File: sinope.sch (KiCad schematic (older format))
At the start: 46 parts, among them J1 PIOA, J2 SERIAL0, J3 PIOB, J4 SERIAL1, J5 Battery, J6 5VDC, Q1 3N3906, SW1 RESET, U1 Z80CPU, U10 MEMORY_GAL, U11 74LS157, U12 TC551001, U2 Z80CTC, U3 Z80PIO, U4 Z80SIO, U5 MAX232, U6 MAX232, U7 IO_GAL, U8 MAX695, U9 27C010, X1 3.6864Mhz

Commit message: PCB mostly routed
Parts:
- removed J4: SERIAL1, Connector_Dsub:DSUB-9_Male_EdgeMount_P2.77mm, symbol Connector:DB9_Male
- added J4: SERIAL1, Connector_PinHeader_2.54mm:PinHeader_1x03_P2.54mm_Vertical, symbol Connector:Conn_01x03_Male
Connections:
- wire segments 410 -> 405
- no-connect marks 37 -> 31
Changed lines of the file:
@@
 $Descr A3 16535 11693
 encoding utf-8
-Sheet 1 2
+Sheet 1 1
 Title "sinope Z80 Single Board Computer"
 Date "2020-04-16"
@@
 	1    0    0    -1
 $EndComp
-NoConn ~ 15200 4000
-NoConn ~ 15200 3900
-NoConn ~ 15200 3700
-NoConn ~ 15200 3500
-NoConn ~ 15200 3400
-NoConn ~ 15200 3300
 NoConn ~ 15200 2200
 NoConn ~ 15200 1600
@@
 	14000 2200 14100 2200
 Wire Wire Line
-	14900 1700 14900 3900
-Wire Wire Line
-	14900 1700 15200 1700
-Wire Wire Line
 	14000 2100 15200 2100
 Wire Wire Line
@@
 Wire Wire Line
 	14000 1900 15200 1900
-Wire Wire Line
-	15000 2300 15000 4100
-Wire Wire Line
-	15000 2300 15200 2300
-Wire Wire Line
-	14750 3200 15200 3200
-$Comp
-L power:GND #PWR019
-U 1 1 5F911907
-P 14750 3200
-F 0 "#PWR019" H 14750 2950 50  0001 C CNN
-F 1 "GND" H 14750 3050 50  0000 C CNN
-F 2 "" H 14750 3200 50  0001 C CNN
-F 3 "" H 14750 3200 50  0001 C CNN
-	1    14750 3200
-	1    0    0    -1
-$EndComp
 Text Label 14350 4200 2    50   ~ 0
 RxDB
 Text Label 14350 4000 2    50   ~ 0
 TxDB
-Wire Wire Line
-	14800 3600 15200 3600
-Wire Wire Line
-	14800 4000 14800 3600
-Wire Wire Line
-	14000 4000 14800 4000
-Wire Wire Line
-	15100 3800 15200 3800
-Wire Wire Line
-	15100 4200 15100 3800
-Wire Wire Line
-	14000 4200 15100 4200
 Text Label 14350 3900 2    50   ~ 0
 DTRA
@@
 Wire Wire Line
 	14000 4100 15000 4100
-$Comp
-L Connector:DB9_Male J4
-U 1 1 5F8AE309
-P 15500 3600
-F 0 "J4" H 15680 3646 50  0000 L CNN
-F 1 "SERIAL1" H 15680 3555 50  0000 L CNN
-F 2 "Connector_Dsub:DSUB-9_Male_EdgeMount_P2.77mm" H 15500 3600 50  0001 C CNN
-F 3 " ~" H 15500 3600 50  0001 C CNN
-	1    15500 3600
-	1    0    0    -1
-$EndComp
 $Comp
 L Connector:DB9_Male J2
@@
 Wire Wire Line
 	12900 3300 12900 3200
-Wire Wire Line
-	13100 3300 12900 3300
 Wire Wire Line
 	12900 3400 13100 3400
@@
 Wire Wire Line
 	1250 3000 1850 3000
-Text GLabel 12600 9150 0    50   Input ~ 0
+Text GLabel 13950 9150 2    50   Input ~ 0
 RAMVCC
 Text GLabel 4850 7700 2    50   Output ~ 0
@@
 	11800 2300 12500 2300
 Wire Wire Line
-	12500 2300 12500 4200
-Wire Wire Line
-	12500 4200 13100 4200
-Wire Wire Line
 	11800 2500 12450 2500
-Wire Wire Line
-	12450 2500 12450 4000
-Wire Wire Line
-	12450 4000 13100 4000
 Text GLabel 4700 2100 0    50   Input ~ 0
 ~CTCCS
@@
 Wire Wire Line
 	13050 9150 13050 9350
-Wire Wire Line
-	12600 9150 13050 9150
 Wire Wire Line
 	13050 6550 13050 6500
@@
 	1    0    0    -1
 $EndComp
+Wire Wire Line
+	13850 9150 13950 9150
+Connection ~ 13850 9150
+Wire Wire Line
+	15000 2300 15200 2300
+Wire Wire Line
+	15000 2300 15000 4100
+Wire Wire Line
+	14900 1700 14900 3900
+Wire Wire Line
+	14900 1700 15200 1700
+Wire Wire Line
+	13100 3300 12900 3300
+$Comp
+L Connector:Conn_01x03_Male J4
+U 1 1 5EAC89FF
+P 15400 5000
+F 0 "J4" H 15508 5281 50  0000 C CNN
+F 1 "SERIAL1" H 15508 5190 50  0000 C CNN
+F 2 "Connector_PinHeader_2.54mm:PinHeader_1x03_P2.54mm_Vertical" H 15400 5000 50  0001 C CNN
+F 3 "~" H 15400 5000 50  0001 C CNN
+	1    15400 5000
+	-1   0    0    -1
+$EndComp
+Wire Wire Line
+	12500 4900 15200 4900
+Wire Wire Line
+	12500 2300 12500 4900
+Wire Wire Line
+	12450 5000 15200 5000
+Wire Wire Line
+	12450 2500 12450 5000
+$Comp
+L power:GND #PWR0101
+U 1 1 5ED291FA
+P 15100 5150
+F 0 "#PWR0101" H 15100 4900 50  0001 C CNN
+F 1 "GND" H 15100 5000 50  0000 C CNN
+F 2 "" H 15100 5150 50  0001 C CNN
+F 3 "" H 15100 5150 50  0001 C CNN
+	1    15100 5150
+	1    0    0    -1
+$EndComp
+Wire Wire Line
+	15100 5150 15100 5100
+Wire Wire Line
+	15100 5100 15200 5100
 Wire Bus Line
 	5800 8250 5800 10250

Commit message: PCB routed
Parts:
- removed J2: SERIAL0, Connector_Dsub:DSUB-9_Male_EdgeMount_P2.77mm, symbol Connector:DB9_Male
- added J2: SERIAL0, Connector_PinHeader_2.00mm:PinHeader_2x05_P2.00mm_Vertical, symbol Connector_Generic:Conn_02x05_Top_Bottom
- SW1: footprint Button_Switch_THT:Push_E-Switch_KS01Q01 -> Connector_PinHeader_2.54mm:PinHeader_1x02_P2.54mm_Vertical
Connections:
- net labels removed: RxDB, TxDB
- wire segments 405 -> 412
- no-connect marks 31 -> 36
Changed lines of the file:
@@
 	1    0    0    -1
 $EndComp
-NoConn ~ 15200 2200
-NoConn ~ 15200 1600
-Wire Wire Line
-	14750 1500 15200 1500
 $Comp
 L power:GND #PWR09
 U 1 1 5FA2F101
-P 14750 1500
-F 0 "#PWR09" H 14750 1250 50  0001 C CNN
-F 1 "GND" H 14750 1350 50  0000 C CNN
-F 2 "" H 14750 1500 50  0001 C CNN
-F 3 "" H 14750 1500 50  0001 C CNN
-	1    14750 1500
-	1    0    0    -1
-$EndComp
-Wire Wire Line
-	14100 1800 15200 1800
-Wire Wire Line
-	14100 2200 14100 1800
-Wire Wire Line
-	14000 2200 14100 2200
-Wire Wire Line
-	14000 2100 15200 2100
-Wire Wire Line
-	14000 2000 15200 2000
-Wire Wire Line
-	14000 1900 15200 1900
-Text Label 14350 4200 2    50   ~ 0
-RxDB
-Text Label 14350 4000 2    50   ~ 0
-TxDB
-Text Label 14350 3900 2    50   ~ 0
+P 14550 3100
+F 0 "#PWR09" H 14550 2850 50  0001 C CNN
+F 1 "GND" H 14550 2950 50  0000 C CNN
+F 2 "" H 14550 3100 50  0001 C CNN
+F 3 "" H 14550 3100 50  0001 C CNN
+	1    14550 3100
+	1    0    0    -1
+$EndComp
+Text Label 14250 3900 2    50   ~ 0
 DTRA
-Text Label 14350 4100 2    50   ~ 0
+Text Label 14250 4100 2    50   ~ 0
 DCDA
-Wire Wire Line
-	14000 3900 14900 3900
-Wire Wire Line
-	14000 4100 15000 4100
-$Comp
-L Connector:DB9_Male J2
-U 1 1 5F8ABC1E
-P 15500 1900
-F 0 "J2" H 15680 1946 50  0000 L CNN
-F 1 "SERIAL0" H 15680 1855 50  0000 L CNN
-F 2 "Connector_Dsub:DSUB-9_Male_EdgeMount_P2.77mm" H 15500 1900 50  0001 C CNN
-F 3 " ~" H 15500 1900 50  0001 C CNN
-	1    15500 1900
-	1    0    0    -1
-$EndComp
 Connection ~ 13550 2950
 Wire Wire Line
@@
 P 14200 3300
 F 0 "#PWR020" H 14200 3050 50  0001 C CNN
-F 1 "GND" V 14200 3100 50  0000 C CNN
+F 1 "GND" H 14300 3200 50  0000 C CNN
 F 2 "" H 14200 3300 50  0001 C CNN
 F 3 "" H 14200 3300 50  0001 C CNN
 	1    14200 3300
-	0    -1   -1   0
+	1    0    0    -1
 $EndComp
 $Comp
@@
 Text Label 3400 3800 0    50   ~ 0
 A15
-Text Label 14150 1800 0    50   ~ 0
+Text Label 14050 2200 0    50   ~ 0
 CTSA
-Text Label 14150 1900 0    50   ~ 0
+Text Label 14050 1900 0    50   ~ 0
 TxDA
-Text Label 14150 2000 0    50   ~ 0
+Text Label 14050 2000 0    50   ~ 0
 RTSA
-Text Label 14150 2100 0    50   ~ 0
+Text Label 14050 2100 0    50   ~ 0
 RxDA
 Wire Wire Line
@@
 F 0 "SW1" H 4500 10035 50  0000 C CNN
 F 1 "RESET" H 4500 9944 50  0000 C CNN
-F 2 "Button_Switch_THT:Push_E-Switch_KS01Q01" H 4500 9950 50  0001 C CNN
+F 2 "Connector_PinHeader_2.54mm:PinHeader_1x02_P2.54mm_Vertical" H 4500 9950 50  0001 C CNN
 F 3 "~" H 4500 9950 50  0001 C CNN
 	1    4500 9750
@@
 Connection ~ 13850 9150
 Wire Wire Line
-	15000 2300 15200 2300
-Wire Wire Line
-	15000 2300 15000 4100
-Wire Wire Line
-	14900 1700 14900 3900
-Wire Wire Line
-	14900 1700 15200 1700
-Wire Wire Line
 	13100 3300 12900 3300
 $Comp
@@
 Wire Wire Line
 	15100 5100 15200 5100
+$Comp
+L Connector_Generic:Conn_02x05_Top_Bottom J2
+U 1 1 5EA81F1E
+P 14800 2850
+F 0 "J2" H 14850 3267 50  0000 C CNN
+F 1 "SERIAL0" H 14850 3176 50  0000 C CNN
+F 2 "Connector_PinHeader_2.00mm:PinHeader_2x05_P2.00mm_Vertical" H 14800 2850 50  0001 C CNN
+F 3 "~" H 14800 2850 50  0001 C CNN
+	1    14800 2850
+	1    0    0    -1
+$EndComp
+Wire Wire Line
+	14000 2100 14300 2100
+Wire Wire Line
+	14300 2100 14300 2750
+Wire Wire Line
+	14300 2750 14600 2750
+Wire Wire Line
+	14000 1900 14350 1900
+Wire Wire Line
+	14350 1900 14350 2850
+Wire Wire Line
+	14350 2850 14600 2850
+Wire Wire Line
+	14000 3900 14350 3900
+Wire Wire Line
+	14350 3900 14350 2950
+Wire Wire Line
+	14350 2950 14600 2950
+Wire Wire Line
+	14600 3050 14550 3050
+Wire Wire Line
+	14550 3050 14550 3100
+NoConn ~ 15100 2650
+Wire Wire Line
+	15200 2000 15200 2750
+Wire Wire Line
+	15200 2750 15100 2750
+Wire Wire Line
+	14000 2000 15200 2000
+Wire Wire Line
+	15150 2200 15150 2850
+Wire Wire Line
+	15150 2850 15100 2850
+Wire Wire Line
+	14000 2200 15150 2200
+NoConn ~ 15100 2950
+NoConn ~ 15100 3050
+Wire Wire Line
+	14000 4100 14400 4100
+Wire Wire Line
+	14400 4100 14400 2650
+Wire Wire Line
+	14400 2650 14600 2650
+NoConn ~ 14000 4000
+NoConn ~ 14000 4200
+NoConn ~ 13100 4200
+NoConn ~ 13100 4000
 Wire Bus Line
 	5800 8250 5800 10250

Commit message: Move connectors to one side.
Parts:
- added J7: Z80_BUS, Connector_PinSocket_2.54mm:PinSocket_1x40_P2.54mm_Vertical, symbol sinope:Z80_BUS
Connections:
- wire segments 412 -> 450
- no-connect marks 36 -> 41
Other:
- moved on the sheet: C16, C17, C18, C19, C20, C21, C22, D1, J5, J6, Q1, R2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

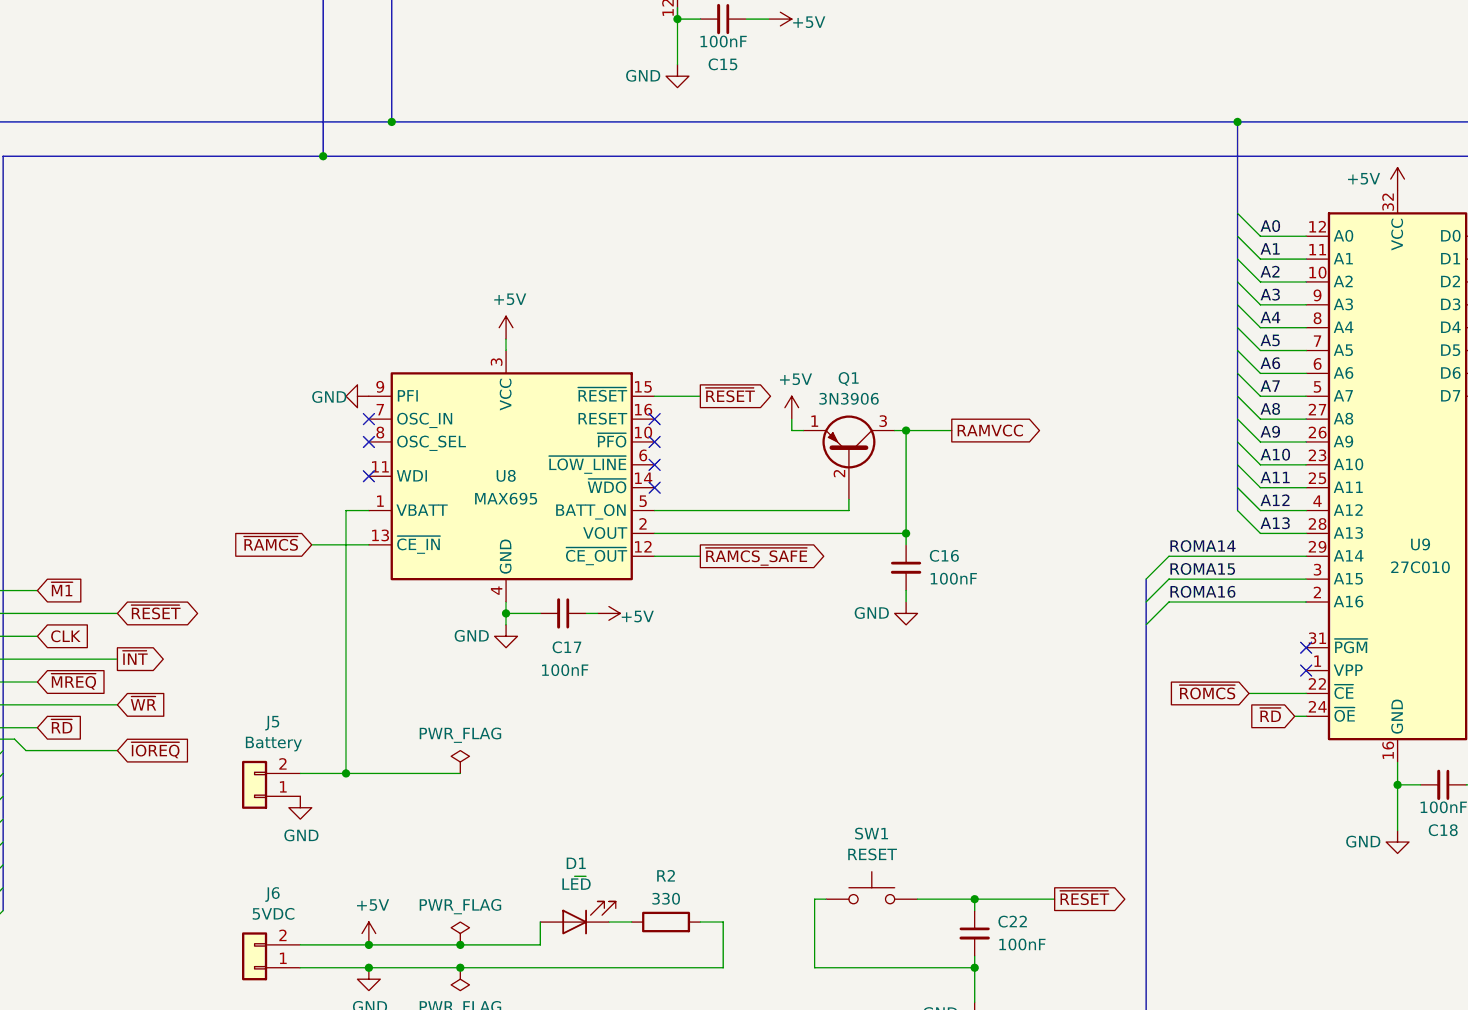
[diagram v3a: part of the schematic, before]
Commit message: ROM variant jumpers and cleanup, sent to JLCPCB for production
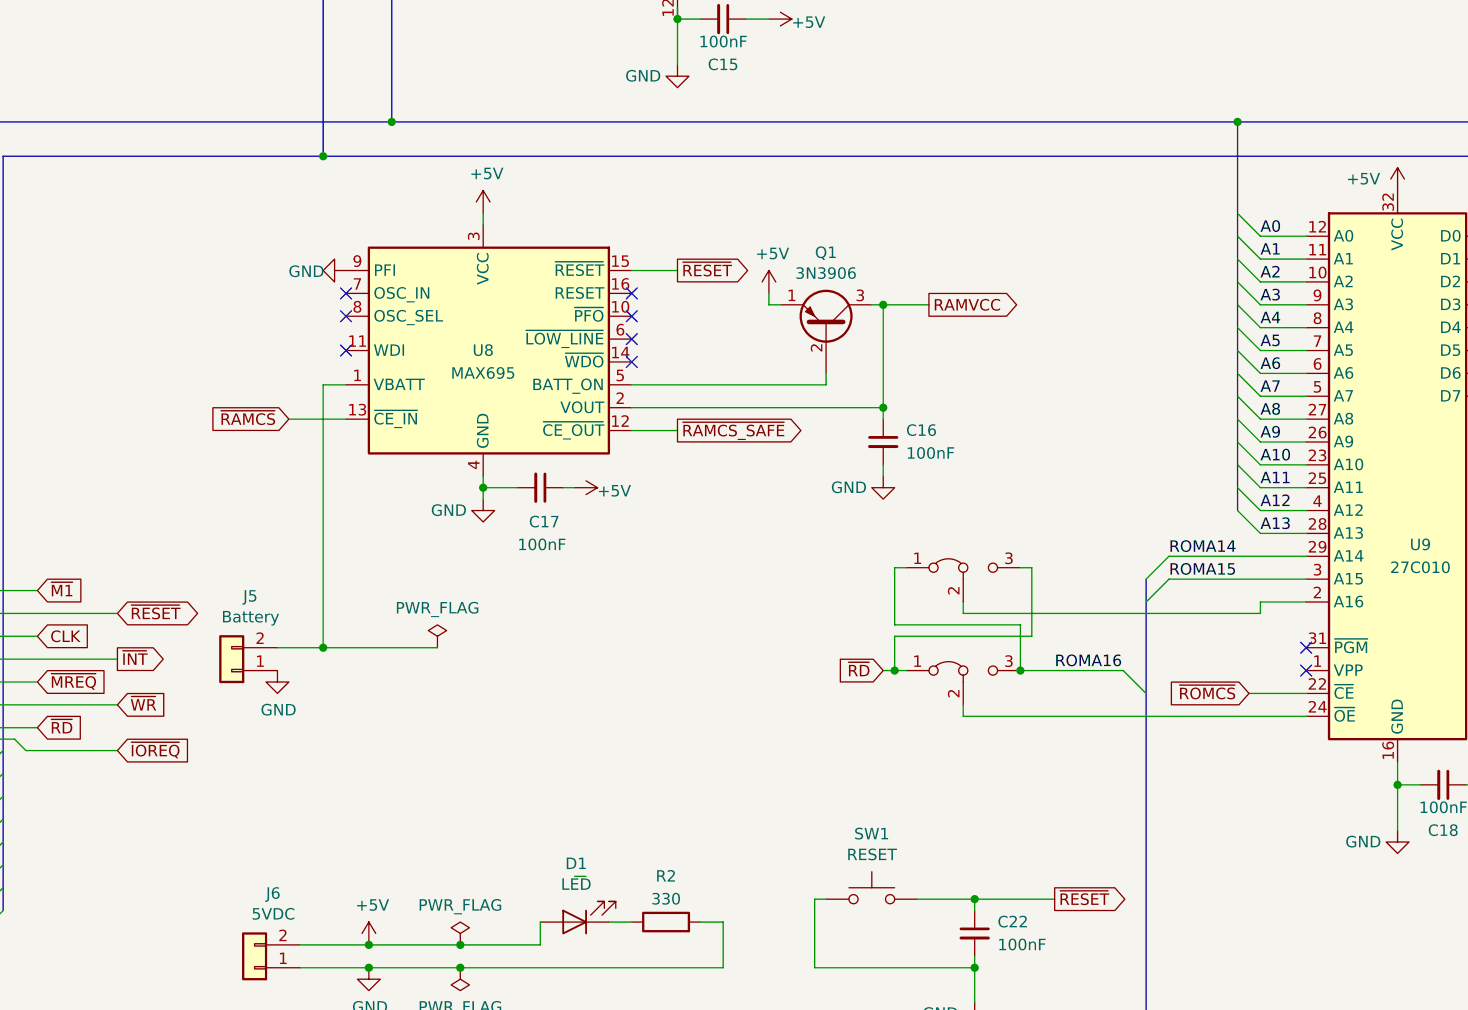
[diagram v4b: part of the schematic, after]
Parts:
- added JP1, JP2: Jumper_3_Bridged12, Connector_PinHeader_2.54mm:PinHeader_1x03_P2.54mm_Vertical, symbol Jumper:Jumper_3_Bridged12
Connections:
- wire segments 450 -> 465
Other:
- moved on the sheet: C16, C17, J5, Q1, U8

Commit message: Begin work on v2
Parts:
- removed C12, C13, C8: 100nF, Capacitor_SMD:C_0805_2012Metric, symbol Device:C_Small
- removed J4: SERIAL1, Connector_PinHeader_2.54mm:PinHeader_1x03_P2.54mm_Vertical, symbol Connector:Conn_01x03_Male
- removed J5: Battery, Connector_PinHeader_2.54mm:PinHeader_2x01_P2.54mm_Vertical, symbol Connector_Generic:Conn_01x02
- removed J6: 5VDC, Connector_PinHeader_2.54mm:PinHeader_1x02_P2.54mm_Vertical, symbol Connector_Generic:Conn_01x02
- removed JP1, JP2: Jumper_3_Bridged12, Connector_PinHeader_2.54mm:PinHeader_1x03_P2.54mm_Vertical, symbol Jumper:Jumper_3_Bridged12
- removed U6: MAX232, Package_DIP:DIP-16_W7.62mm, symbol sinope:MAX232
- added BT1: Battery, Battery:Battery_Panasonic_CR2032-VS1N_Vertical_CircularHoles, symbol Device:Battery_Cell
- added D2, D3: LED, LED_SMD:LED_0805_2012Metric, symbol Device:LED
- added J4: USB_B_Micro, Connector_USB:USB_Micro-B_Molex-105017-0001, symbol Connector:USB_B_Micro
- added JP1, JP2: SolderJumper_3_Bridged12, Connector_PinHeader_2.54mm:PinHeader_1x03_P2.54mm_Vertical, symbol Jumper:SolderJumper_3_Bridged12
- added R3, R4: 330, Resistor_SMD:R_0805_2012Metric, symbol Device:R
- added R5, R6, R7: 3k3, Resistor_SMD:R_0805_2012Metric, symbol Device:R
- added U6: FT232RL, Package_SO:SSOP-28_5.3x10.2mm_P0.65mm, symbol sinope:FT232RL
- J2: value SERIAL0 -> SERIAL1; footprint Connector_PinHeader_2.00mm:PinHeader_2x05_P2.00mm_Vertical -> Connector_PinHeader_2.54mm:PinHeader_2x05_P2.54mm_Vertical
- J7: footprint Connector_PinSocket_2.54mm:PinSocket_1x40_P2.54mm_Vertical -> Connector_PinSocket_2.54mm:PinSocket_1x39_P2.54mm_Vertical
- Q1: value 3N3906 -> MMBT3904; footprint Package_TO_SOT_THT:TO-92 -> Package_TO_SOT_SMD:SOT-23
- SW1: footprint Connector_PinHeader_2.54mm:PinHeader_1x02_P2.54mm_Vertical -> Button_Switch_SMD:SW_SPST_PTS645
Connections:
- net labels added: RxDB, SPARE1, SPARE2, SPARE3, TxDB, USB_D+, USB_D-, ~BUSACK, ~BUSRQ, ~HALT, ~NMI, ~RFSH, ~WAIT
- net labels removed: CTSA, DCDA, DTRA, RTSA, RxDA, TxDA
- wire segments 465 -> 521
- no-connect marks 41 -> 37
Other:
- moved on the sheet: C1, C16, C17, C2, C22, C3, C4, C5, D1, J2, J7, Q1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
